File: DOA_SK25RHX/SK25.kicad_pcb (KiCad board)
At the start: 2 copper layers, 42.5 x 32 mm, 41 parts, among them J1 Input-, J2 Input+, J3 V+, J4 Output, J5 V-, J6 GND, Q1 BC560C, Q10 BD140, Q2 KSA992, Q3 KSA992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

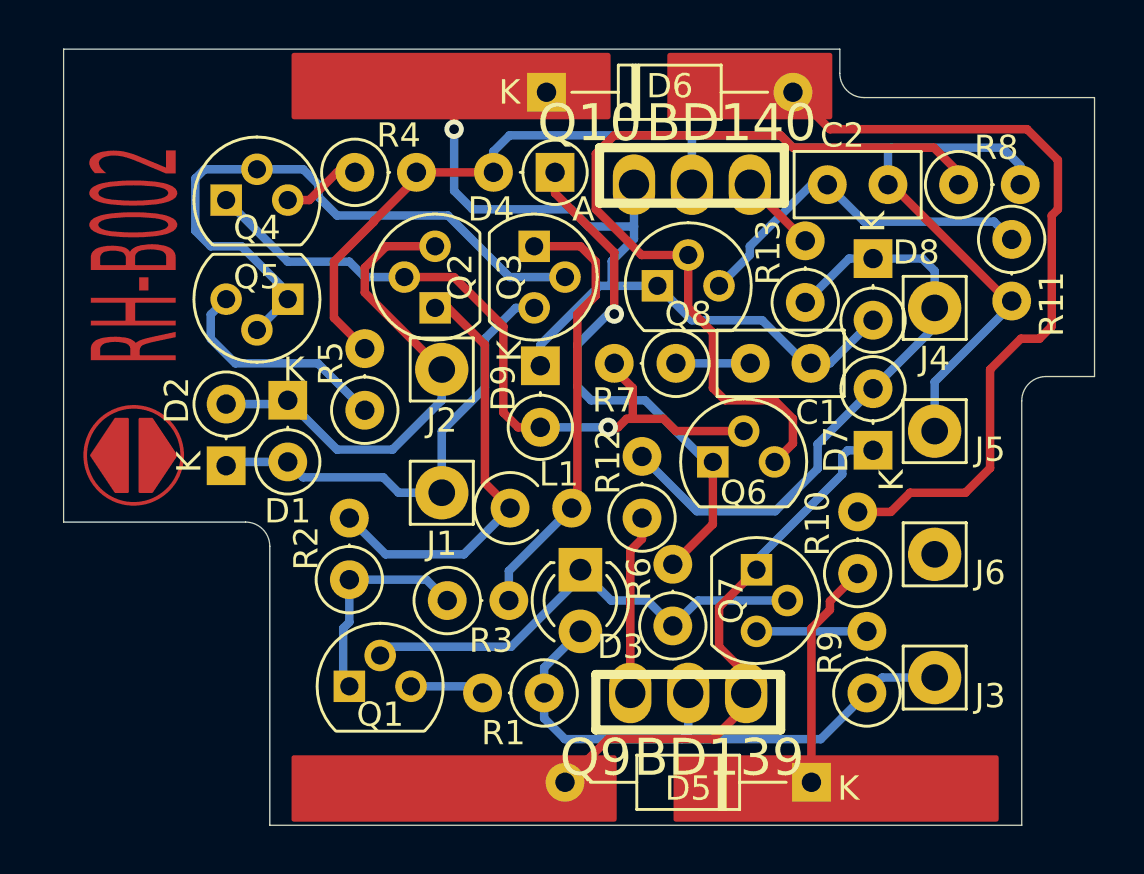
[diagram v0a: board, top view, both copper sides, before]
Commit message: uses copper fill zones
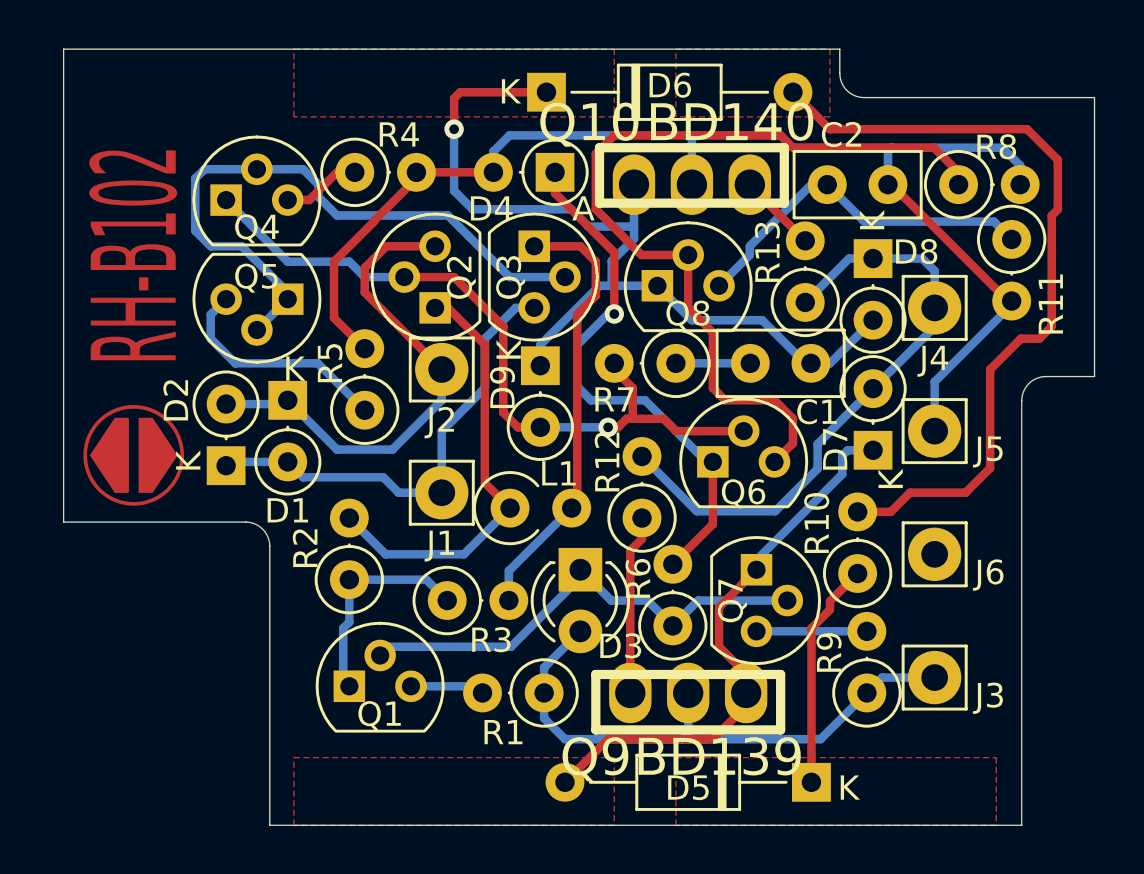
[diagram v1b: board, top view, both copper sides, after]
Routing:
- added copper zone on F.Cu, net Net-(C1-Pad1)
- added copper zone on F.Cu, net Net-(D5-Pad1)
- added copper zone on F.Cu, net Net-(D5-Pad2)
- added copper zone on F.Cu, net Net-(D6-Pad2)
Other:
- board text added: "RH-B102"
- board text removed: "RH-B002"
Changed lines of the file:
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@@
     )
   )
-  (gr_rect (start 158.242 108.712) (end 171.45 111.252) (layer "F.Cu") (width 0.2) (fill solid))
   (gr_poly
     (pts
@@
       (xy 134.14 96.25)
     ) (layer "F.Cu") (width 0.1) (fill solid))
-  (gr_rect (start 142.494 79.756) (end 155.448 82.296) (layer "F.Cu") (width 0.2) (fill solid))
   (gr_poly
     (pts
@@
       (xy 136.14 94.75)
     ) (layer "F.Cu") (width 0.1) (fill solid))
-  (gr_rect (start 142.494 108.712) (end 155.702 111.252) (layer "F.Cu") (width 0.2) (fill solid))
   (gr_circle (center 135.89 96.25) (end 137.89 96.25) (layer "F.Cu") (width 0.15) (fill none))
-  (gr_rect (start 157.988 79.756) (end 164.592 82.296) (layer "F.Cu") (width 0.2) (fill solid))
+  (gr_line (start 159.131 98.552) (end 162.306 98.552) (layer "B.Mask") (width 0.4))
+  (gr_line (start 164.211 107.95) (end 158.75 107.95) (layer "B.Mask") (width 0.35))
+  (gr_line (start 166.751 105.41) (end 164.211 107.95) (layer "B.Mask") (width 0.35))
+  (gr_line (start 159.131 98.552) (end 157.226 96.647) (layer "B.Mask") (width 0.4))
+  (gr_line (start 165.354 88.138) (end 168.402 88.138) (layer "B.Mask") (width 0.4))
+  (gr_line (start 167.894 105.41) (end 166.751 105.41) (layer "B.Mask") (width 0.35))
+  (gr_line (start 168.91 93.218) (end 171.577 90.551) (layer "B.Mask") (width 0.4))
+  (gr_line (start 162.56 83.058) (end 158.877 83.058) (layer "B.Mask") (width 0.4))
+  (gr_line (start 168.91 88.646) (end 168.91 89.154) (layer "B.Mask") (width 0.4))
+  (gr_line (start 163.068 83.566) (end 162.56 83.058) (layer "B.Mask") (width 0.4))
+  (gr_line (start 168.91 94.107) (end 168.91 93.218) (layer "B.Mask") (width 0.4))
+  (gr_line (start 164.084 96.774) (end 164.084 95.758) (layer "B.Mask") (width 0.4))
+  (gr_line (start 167.005 84.455) (end 167.005 83.566) (layer "B.Mask") (width 0.4))
+  (gr_line (start 168.402 88.138) (end 168.91 88.646) (layer "B.Mask") (width 0.4))
+  (gr_line (start 158.877 83.058) (end 158.877 83.947) (layer "B.Mask") (width 0.4))
+  (gr_line (start 162.306 98.552) (end 164.084 96.774) (layer "B.Mask") (width 0.4))
+  (gr_line (start 167.005 83.566) (end 163.068 83.566) (layer "B.Mask") (width 0.4))
+  (gr_line (start 165.354 88.138) (end 164.084 89.408) (layer "B.Mask") (width 0.4))
+  (gr_line (start 158.75 107.061) (end 158.75 107.95) (layer "B.Mask") (width 0.35))
+  (gr_line (start 164.084 95.758) (end 168.656 91.186) (layer "B.Mask") (width 0.4))
+  (gr_line (start 156.845 99.695) (end 156.845 99.441) (layer "F.Mask") (width 0.4))
+  (gr_line (start 156.337 100.203) (end 156.845 99.695) (layer "F.Mask") (width 0.4))
+  (gr_line (start 163.068 86.868) (end 162.052 85.852) (layer "F.Mask") (width 0.4))
+  (gr_line (start 156.337 104.775) (end 156.337 100.203) (layer "F.Mask") (width 0.4))
+  (gr_line (start 167.64 85.598) (end 171.45 89.408) (layer "F.Mask") (width 0.4))
   (gr_rect (start 171.5 83.5) (end 142.5 82) (layer "Dwgs.User") (width 0.1) (fill none))
   (gr_rect (start 171.5 109) (end 142.5 107.5) (layer "Dwgs.User") (width 0.1) (fill none))
@@
   (gr_line (start 175.5 93) (end 175.5 81.5) (layer "Edge.Cuts") (width 0.05))
   (gr_line (start 165 79.502) (end 133 79.502) (layer "Edge.Cuts") (width 0.05))
-  (gr_text "RH-B002" (at 136 88 90) (layer "F.Cu")
+  (gr_text "RH-B102" (at 136 88 90) (layer "F.Cu")
     (effects (font (size 3.5 1.5) (thickness 0.35)))
   )
@@
   (segment (start 171.196 96.774) (end 170.18 97.79) (width 0.35) (layer "F.Cu") (net 12))
   (segment (start 165.383 88.138) (end 166.37 88.138) (width 0.35) (layer "B.Cu") (net 13))
-  (segment (start 166.37 93.500686) (end 168.91 90.960686) (width 0.35) (layer "B.Cu") (net 13))
+  (segment (start 164.084 95.786686) (end 166.37 93.500686) (width 0.35) (layer "B.Cu") (net 13))
   (segment (start 168.402 88.138) (end 168.91 88.646) (width 0.35) (layer "B.Cu") (net 13))
   (segment (start 164.084 96.804878) (end 164.084 95.786686) (width 0.35) (layer "B.Cu") (net 13))
+  (segment (start 166.37 93.500686) (end 168.91 90.960686) (width 0.35) (layer "B.Cu") (net 13))
   (segment (start 156.845 96.295) (end 159.102 98.552) (width 0.35) (layer "B.Cu") (net 13))
-  (segment (start 164.084 95.786686) (end 166.37 93.500686) (width 0.35) (layer "B.Cu") (net 13))
+  (segment (start 168.91 90.960686) (end 168.91 90.17) (width 0.35) (layer "B.Cu") (net 13))
   (segment (start 168.91 88.646) (end 168.91 90.17) (width 0.35) (layer "B.Cu") (net 13))
   (segment (start 162.336878 98.552) (end 164.084 96.804878) (width 0.35) (layer "B.Cu") (net 13))
   (segment (start 163.576 89.945) (end 165.383 88.138) (width 0.35) (layer "B.Cu") (net 13))
-  (segment (start 168.91 90.960686) (end 168.91 90.17) (width 0.35) (layer "B.Cu") (net 13))
   (segment (start 166.37 88.138) (end 168.402 88.138) (width 0.35) (layer "B.Cu") (net 13))
   (segment (start 159.102 98.552) (end 162.336878 98.552) (width 0.35) (layer "B.Cu") (net 13))
@@
   (segment (start 161.29 85.09) (end 161.29 85.119) (width 0.35) (layer "F.Cu") (net 25))
   (segment (start 161.29 85.119) (end 163.576 87.405) (width 0.35) (layer "F.Cu") (net 25))
-  (zone (net 0) (net_name "") (layer "F.Mask") (hatch edge 0.508)
-    (connect_pads (clearance 0.508))
-    (min_thickness 0.254) (filled_areas_thickness no)
-    (fill yes (thermal_gap 0.508) (thermal_bridge_width 0.508) (smoothing chamfer))
+  (zone (net 12) (net_name "Net-(D6-Pad2)") (layer "F.Cu") (hatch edge 0.508)
+    (connect_pads yes (clearance 0.1))
+    (min_thickness 0.254) (filled_areas_thickness no)
+    (fill yes (thermal_gap 0.508) (thermal_bridge_width 0.508) (smoothing fillet) (radius 0.2) (island_removal_mode 1) (island_area_min 0))
     (polygon
       (pts
         (xy 164.592 82.296)
-        (xy 157.988 82.296)
-        (xy 157.988 79.502)
+        (xy 158.242 82.296)
+        (xy 158.242 79.502)
         (xy 164.592 79.502)
       )
     )
   )
-  (zone (net 0) (net_name "") (layer "F.Mask") (hatch edge 0.508)
-    (connect_pads (clearance 0.508))
-    (min_thickness 0.254) (filled_areas_thickness no)
-    (fill yes (thermal_gap 0.508) (thermal_bridge_width 0.508) (smoothing chamfer))
-    (polygon
-      (pts
-        (xy 155.448 82.296)
-        (xy 142.494 82.296)
-        (xy 142.494 79.502)
-        (xy 155.448 79.502)
-      )
-    )
-  )
-  (zone (net 0) (net_name "") (layer "F.Mask") (hatch edge 0.508)
-    (connect_pads (clearance 0.508))
-    (min_thickness 0.254) (filled_areas_thickness no)
-    (fill yes (thermal_gap 0.508) (thermal_bridge_width 0.508) (smoothing chamfer))
+  (zone (net 11) (net_name "Net-(D5-Pad1)") (layer "F.Cu") (hatch edge 0.508)
+    (connect_pads yes (clearance 0.1))
+    (min_thickness 0.254) (filled_areas_thickness no)
+    (fill yes (thermal_gap 0.508) (thermal_bridge_width 0.508) (smoothing fillet) (radius 0.2))
+    (polygon
+      (pts
+        (xy 171.45 111.506)
+        (xy 158.242 111.506)
+        (xy 158.242 108.712)
+        (xy 171.45 108.712)
+      )
+    )
+  )
+  (zone (net 10) (net_name "Net-(D5-Pad2)") (layer "F.Cu") (hatch edge 0.508)
+    (connect_pads yes (clearance 0.1))
+    (min_thickness 0.254) (filled_areas_thickness no)
+    (fill yes (thermal_gap 0.508) (thermal_bridge_width 0.508) (smoothing fillet) (radius 0.2))
     (polygon
       (pts
@@
     )
   )
+  (zone (net 2) (net_name "Net-(C1-Pad1)") (layer "F.Cu") (hatch edge 0.508)
+    (connect_pads yes (clearance 0.1))
+    (min_thickness 0.254) (filled_areas_thickness no)
+    (fill yes (thermal_gap 0.508) (thermal_bridge_width 0.508) (smoothing fillet) (radius 0.2) (island_removal_mode 1) (island_area_min 0))
+    (polygon
+      (pts
+        (xy 155.702 82.296)
+        (xy 142.494 82.296)
+        (xy 142.494 79.502)
+        (xy 155.702 79.502)
+      )
+    )
+  )
   (zone (net 0) (net_name "") (layer "F.Mask") (hatch edge 0.508)
     (connect_pads (clearance 0.508))
     (min_thickness 0.254) (filled_areas_thickness no)
+    (fill yes (thermal_gap 0.508) (thermal_bridge_width 0.508) (smoothing fillet) (radius 0.2))
+    (polygon
+      (pts
+        (xy 164.592 82.296)
+        (xy 158.242 82.296)
+        (xy 158.242 79.248)
+        (xy 164.592 79.248)
+      )
+    )
+  )
+  (zone (net 0) (net_name "") (layer "F.Mask") (hatch edge 0.508)
+    (connect_pads (clearance 0.508))
+    (min_thickness 0.254) (filled_areas_thickness no)
+    (fill yes (thermal_gap 0.508) (thermal_bridge_width 0.508) (smoothing fillet) (radius 0.2))
+    (polygon
+      (pts
+        (xy 155.702 82.296)
+        (xy 142.494 82.296)
+        (xy 142.494 79.248)
+        (xy 155.702 79.248)
+      )
+    )
+  )
+  (zone (net 0) (net_name "") (layer "F.Mask") (hatch edge 0.508)
+    (connect_pads (clearance 0.508))
+    (min_thickness 0.254) (filled_areas_thickness no)
     (fill yes (thermal_gap 0.508) (thermal_bridge_width 0.508) (smoothing chamfer))
     (polygon
       (pts
-        (xy 171.45 111.506)
-        (xy 158.242 111.506)
+        (xy 155.702 111.76)
+        (xy 142.494 111.76)
+        (xy 142.494 108.712)
+        (xy 155.702 108.712)
+      )
+    )
+  )
+  (zone (net 0) (net_name "") (layer "F.Mask") (hatch edge 0.508)
+    (connect_pads (clearance 0.508))
+    (min_thickness 0.254) (filled_areas_thickness no)
+    (fill yes (thermal_gap 0.508) (thermal_bridge_width 0.508) (smoothing chamfer))
+    (polygon
+      (pts
+        (xy 171.45 111.76)
+        (xy 158.242 111.76)
         (xy 158.242 108.712)
         (xy 171.45 108.712)

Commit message: modified BJT footprints
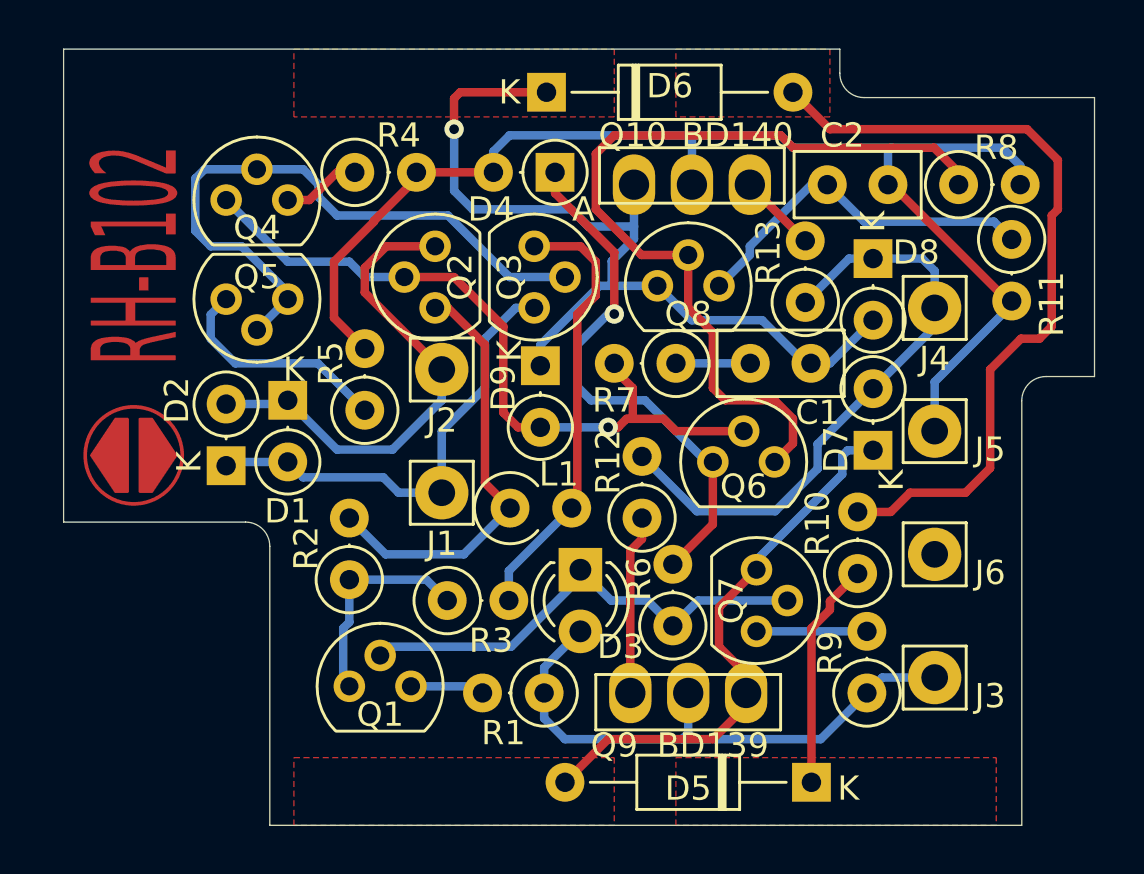
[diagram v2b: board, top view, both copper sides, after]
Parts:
- Q1, Q2, Q3, Q4, Q5, Q6, Q7, Q8: footprint Package_TO_SOT_THT:TO-92 -> TAC:TO-92
